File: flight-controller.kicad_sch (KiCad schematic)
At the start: 84 parts, among them J1 USB_C_Receptacle_USB2.0, J2 ESC, J3 RX, J4 GPS, J5 I2C, J6 Camera, J7 VTX, J8 DVTX, Q1 AO3400A, SW1 SW_Push, U1 AT32F435RGT7, U2 BMI270, U3 BMP280, U4 W25N01GVZEIG, U5 AT7456E, U6 TPS54302, U7 TPS54302, U8 TLV75733PDBV, U9 USBLC6-2P6, Y1 27MHz, Y2 8MHz

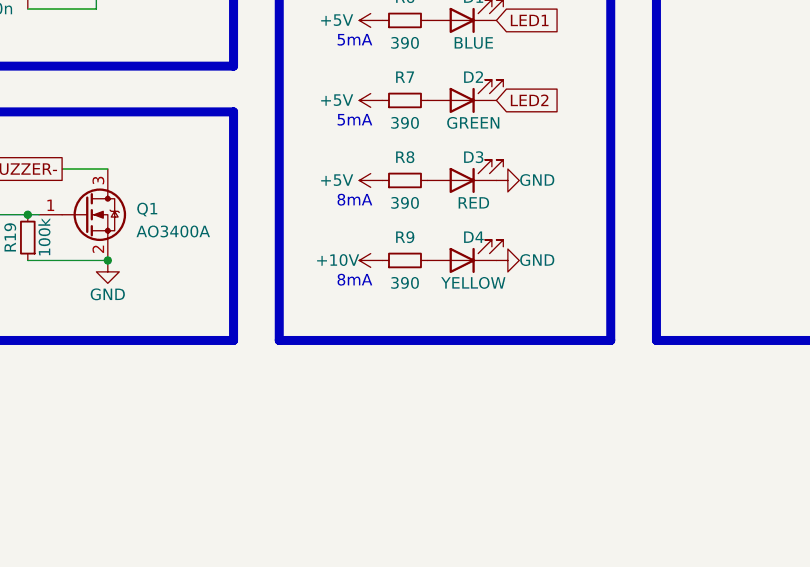
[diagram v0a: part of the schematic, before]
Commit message: Fix LED resistor value
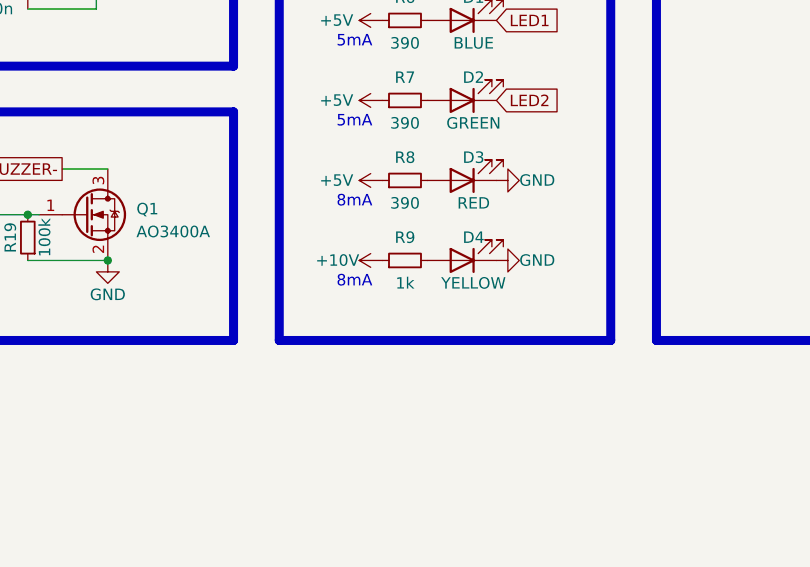
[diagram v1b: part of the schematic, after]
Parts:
- R9: value 390 -> 1k; LCSC C23151 -> C21190
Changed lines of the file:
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@@
       (effects (font (size 1.27 1.27)))
     )
-    (property "Value" "390" (at 307.34 146.05 90)
+    (property "Value" "1k" (at 307.34 146.05 90)
       (effects (font (size 1.27 1.27)))
     )
@@
       (effects (font (size 1.27 1.27)) hide)
     )
-    (property "LCSC" "C23151" (at 307.34 143.51 90)
+    (property "LCSC" "C21190" (at 307.34 143.51 90)
       (effects (font (size 1.27 1.27)) hide)
     )

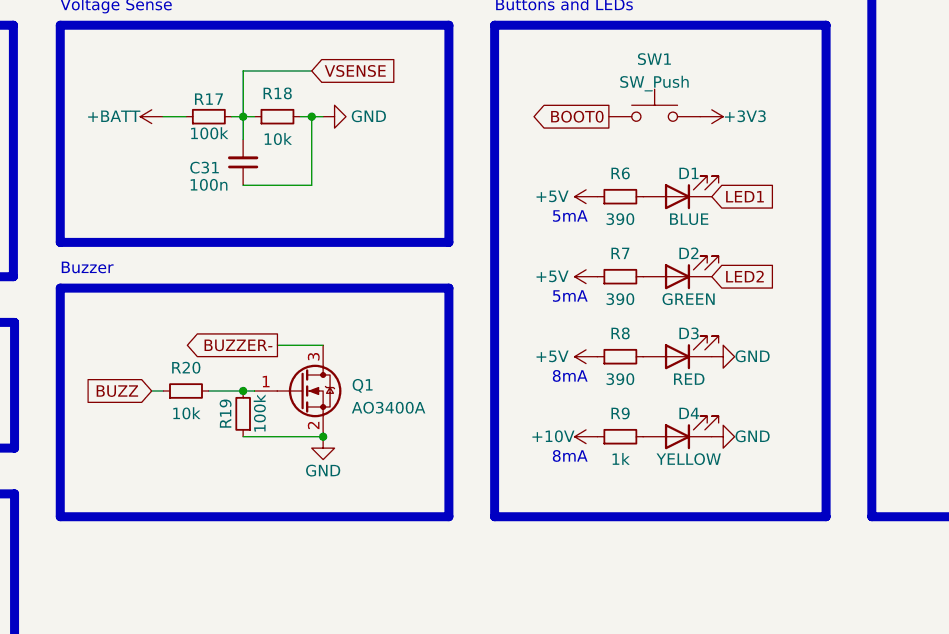
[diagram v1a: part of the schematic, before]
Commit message: Change LED resistors again
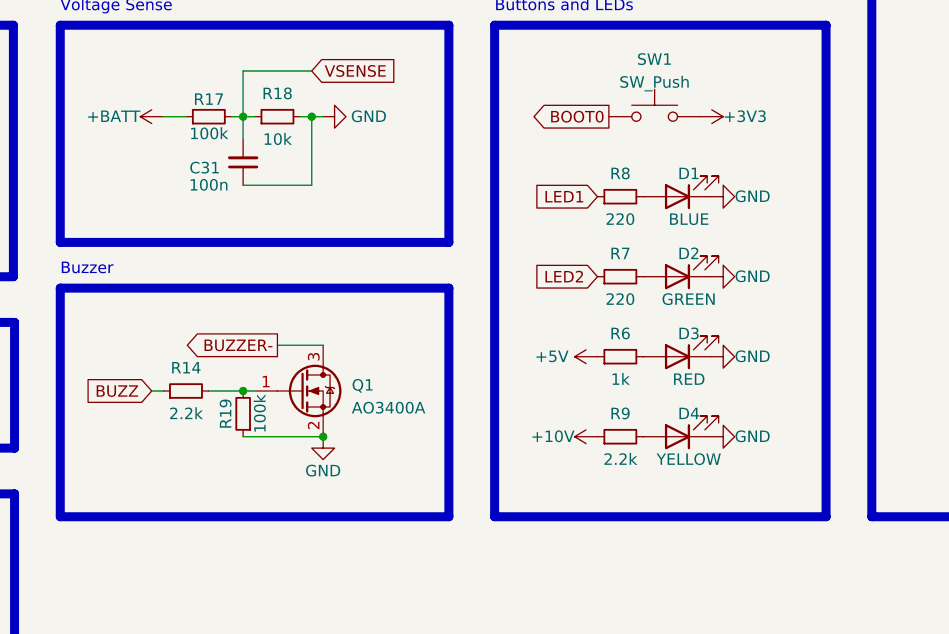
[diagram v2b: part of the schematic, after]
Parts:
- removed R20: 10k, Resistor_SMD:R_0402_1005Metric, symbol Device:R_Small
- added R14: 2.2k, Resistor_SMD:R_0603_1608Metric, symbol Device:R_Small
- R6: value 390 -> 1k; LCSC C23151 -> C21190
- R7, R8: value 390 -> 220; LCSC C23151 -> C22962
- R9: value 1k -> 2.2k; LCSC C21190 -> C4190
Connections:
- net +5V: no longer R7.1, R8.1
- net BUZZ: now also R14.1
- net GND: now also D1.1 (K), D2.1 (K)
- net LED1: now also R8.1; no longer D1.1 (K)
- net LED2: now also R7.1; no longer D2.1 (K)
- net at D3.2 (A): now also R6.2; no longer R8.2
- net at D1.2 (A): now also R8.2; no longer R6.2
- net at Q1.1 (G), R19.2: now also R14.2
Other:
- note removed: "5mA"
- note removed: "8mA"

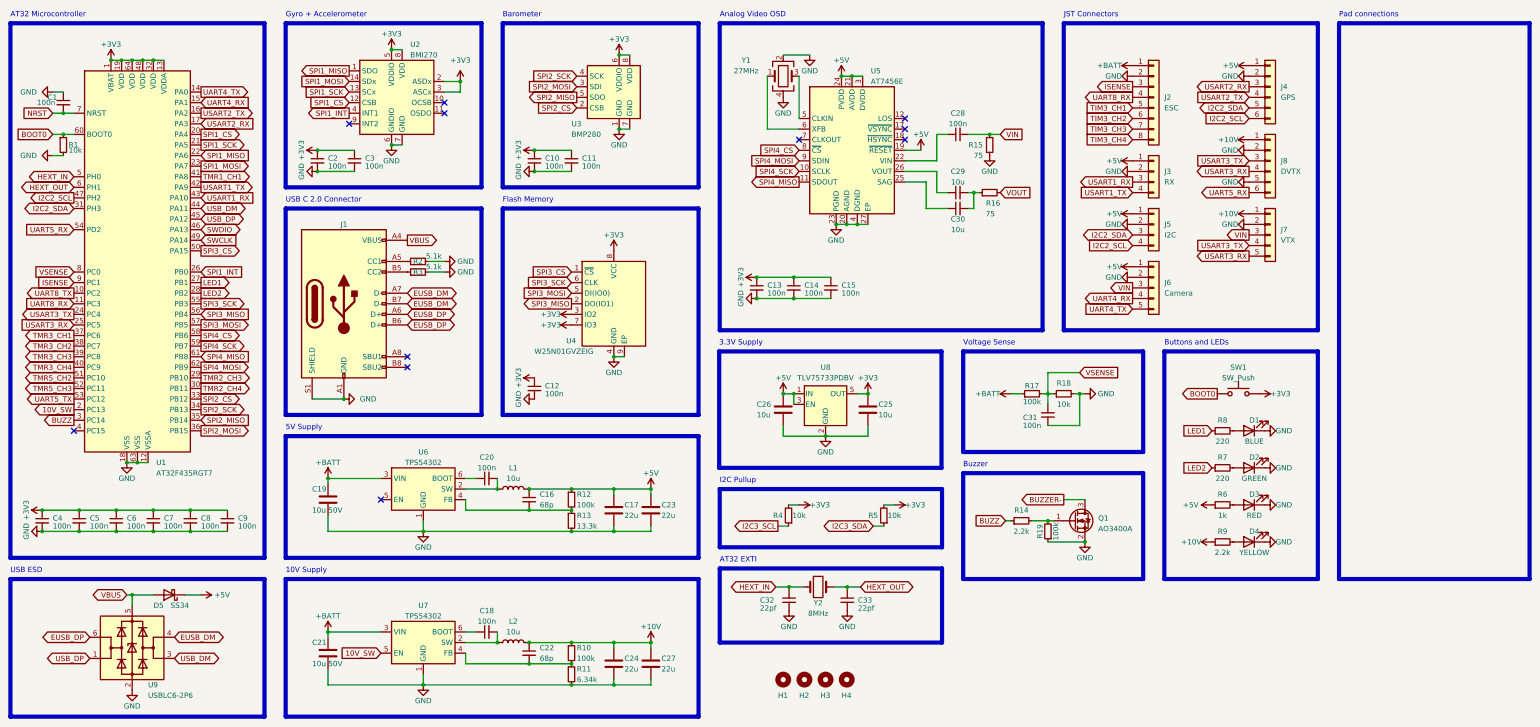
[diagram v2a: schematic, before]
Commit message: Change baro to I2C
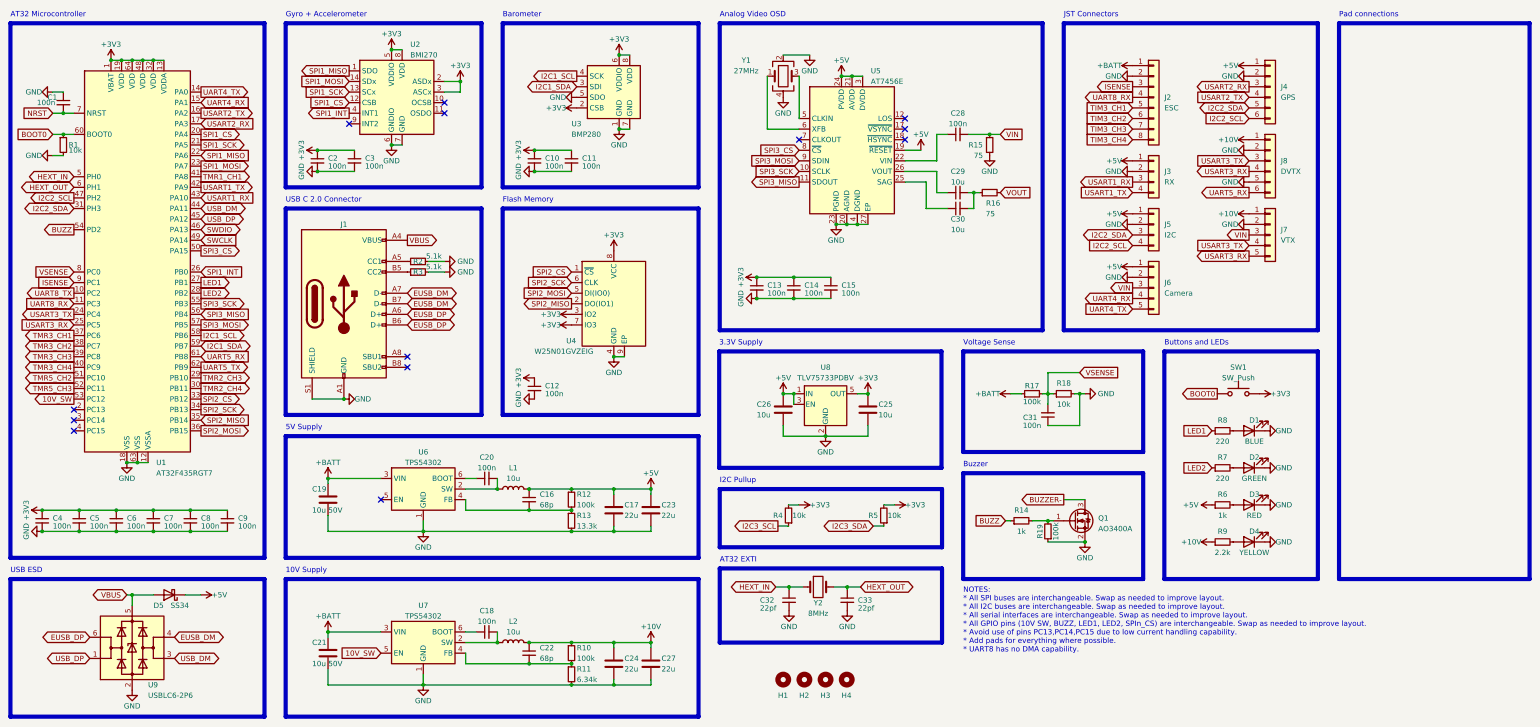
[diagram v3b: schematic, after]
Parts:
- R14: value 2.2k -> 1k; LCSC C4190 -> C21190
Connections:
- net +3V3: now also U3.2 (CSB)
- net 10V_SW: now also U1.53 (PC12); no longer U1.2 (PC13)
- net BUZZ: now also U1.54 (PD2); no longer U1.3 (PC14)
- net GND: now also U3.5 (SDO)
- net SPI2_CS: now also U4.1 (~{CS}); no longer U3.2 (CSB)
- net SPI2_MISO: now also U4.2 (DO(IO1)); no longer U3.5 (SDO)
- net SPI2_MOSI: now also U4.5 (DI(IO0)); no longer U3.3 (SDI)
- net SPI2_SCK: now also U4.6 (CLK); no longer U3.4 (SCK)
- net SPI3_CS: now also U5.8 (~{CS}); no longer U4.1 (~{CS})
- net SPI3_MISO: now also U5.11 (SDOUT); no longer U4.2 (DO(IO1))
- net SPI3_MOSI: now also U5.9 (SDIN); no longer U4.5 (DI(IO0))
- net SPI3_SCK: now also U5.10 (SCLK); no longer U4.6 (CLK)
- net UART5_RX: now also U1.61 (PB8); no longer U1.54 (PD2)
- net UART5_TX: now also U1.62 (PB9); no longer U1.53 (PC12)
- net SPI4_CS renamed I2C1_SCL
- net I2C1_SCL: now also U3.4 (SCK); no longer U5.8 (~{CS})
- removed net SPI4_MISO: U1.61 (PB8), U5.11 (SDOUT)
- removed net SPI4_MOSI: U1.62 (PB9), U5.9 (SDIN)
- net SPI4_SCK renamed I2C1_SDA
- net I2C1_SDA: now also U3.3 (SDI); no longer U5.10 (SCLK)
- no-connect marks 11 -> 13
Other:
- note added: "NOTES: * All SPI buses are interchangeable. Swap as needed to improve layout. * All I2C buses are interchangeable. Swap as needed to improve layout. * All serial interfaces are interchangeable. Swap as needed to improve layout. * All GPIO pins (10V SW, BUZZ, LED1, LED2, SPIn_CS) are interchangeable. Swap as needed to improve layout. * Avoid use of pins PC13,PC14,PC15 due to low current handling c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"

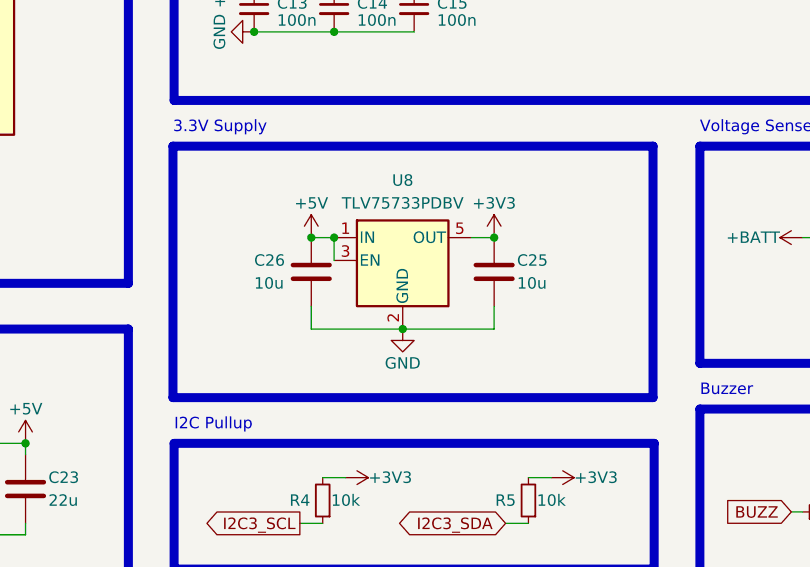
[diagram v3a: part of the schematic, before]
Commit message: Reduce size of 3v3 regulator capacitors
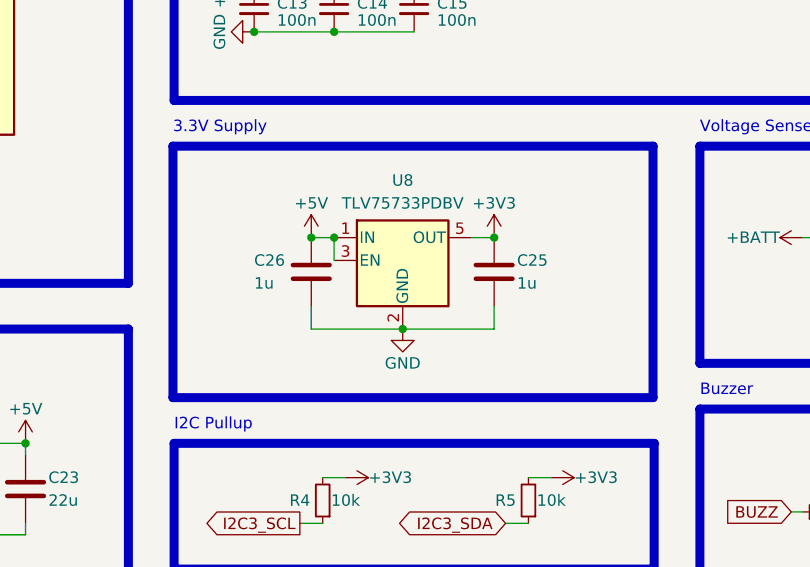
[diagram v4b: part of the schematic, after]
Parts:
- C25, C26: value 10u -> 1u; footprint Capacitor_SMD:C_0603_1608Metric -> Capacitor_SMD:C_0402_1005Metric; LCSC C19702 -> C52923
- R14: footprint Resistor_SMD:R_0603_1608Metric -> Resistor_SMD:R_0402_1005Metric; LCSC C21190 -> C11702
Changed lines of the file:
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@@
       (effects (font (size 1.27 1.27)) (justify left))
     )
-    (property "Value" "10u" (at 195.58 113.03 0)
-      (effects (font (size 1.27 1.27)) (justify left))
-    )
-    (property "Footprint" "Capacitor_SMD:C_0603_1608Metric" (at 202.8952 115.57 0)
+    (property "Value" "1u" (at 195.58 113.03 0)
+      (effects (font (size 1.27 1.27)) (justify left))
+    )
+    (property "Footprint" "Capacitor_SMD:C_0402_1005Metric" (at 202.8952 115.57 0)
       (effects (font (size 1.27 1.27)) hide)
     )
@@
       (effects (font (size 1.27 1.27)) hide)
     )
-    (property "LCSC" "C19702" (at 201.93 111.76 0)
+    (property "LCSC" "C52923" (at 201.93 111.76 0)
       (effects (font (size 1.27 1.27)) hide)
     )
@@
       (effects (font (size 1.27 1.27)) (justify left))
     )
-    (property "Value" "10u" (at 224.79 113.03 0)
-      (effects (font (size 1.27 1.27)) (justify left))
-    )
-    (property "Footprint" "Capacitor_SMD:C_0603_1608Metric" (at 223.2152 115.57 0)
+    (property "Value" "1u" (at 224.79 113.03 0)
+      (effects (font (size 1.27 1.27)) (justify left))
+    )
+    (property "Footprint" "Capacitor_SMD:C_0402_1005Metric" (at 223.2152 115.57 0)
       (effects (font (size 1.27 1.27)) hide)
     )
@@
       (effects (font (size 1.27 1.27)) hide)
     )
-    (property "LCSC" "C19702" (at 222.25 111.76 0)
+    (property "LCSC" "C52923" (at 222.25 111.76 0)
       (effects (font (size 1.27 1.27)) hide)
     )
@@
       (effects (font (size 1.27 1.27)))
     )
-    (property "Footprint" "Resistor_SMD:R_0603_1608Metric" (at 259.08 138.43 0)
+    (property "Footprint" "Resistor_SMD:R_0402_1005Metric" (at 259.08 138.43 0)
       (effects (font (size 1.27 1.27)) hide)
     )
@@
       (effects (font (size 1.27 1.27)) hide)
     )
-    (property "LCSC" "C21190" (at 259.08 138.43 90)
-      (effects (font (size 1.27 1.27)) hide)
-    )
+    (property "LCSC" "C11702" (at 259.08 138.43 90)
+      (effects (font (size 1.27 1.27)) hide)
+    )
